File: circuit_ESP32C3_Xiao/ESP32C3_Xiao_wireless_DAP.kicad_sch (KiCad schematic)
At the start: 41 parts, among them J1 Cortex Debug 10pin connector, J2 ARM Standard JTAG, J3 Cortex Debug 10pin connector, J4 Conn_01x02, J6 Serial, Q1 ZXM61N03F, U1 XIAO-ESP32-C3-SMD, U2 AP1117-ADJ

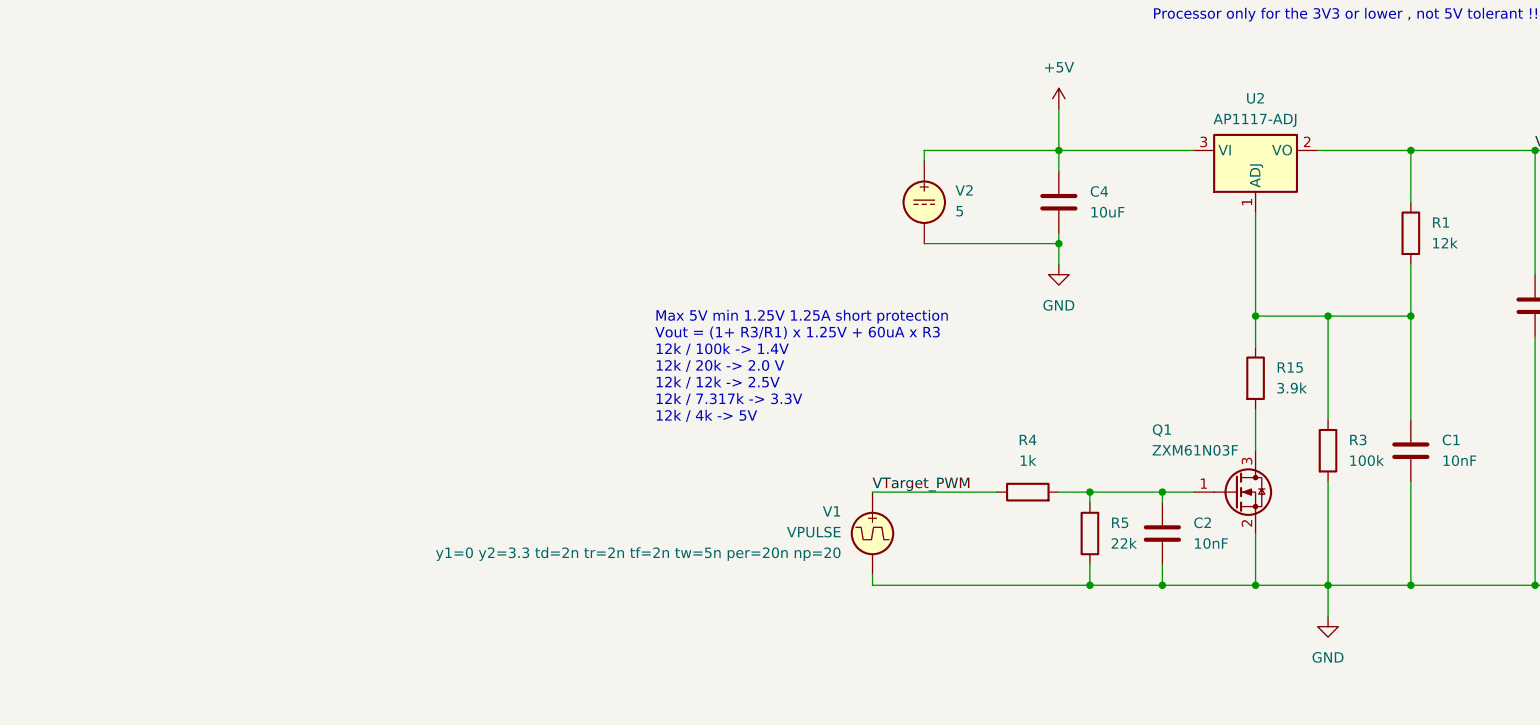
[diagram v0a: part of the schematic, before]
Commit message: Update the circuit, and create proper SPICE simulation model.
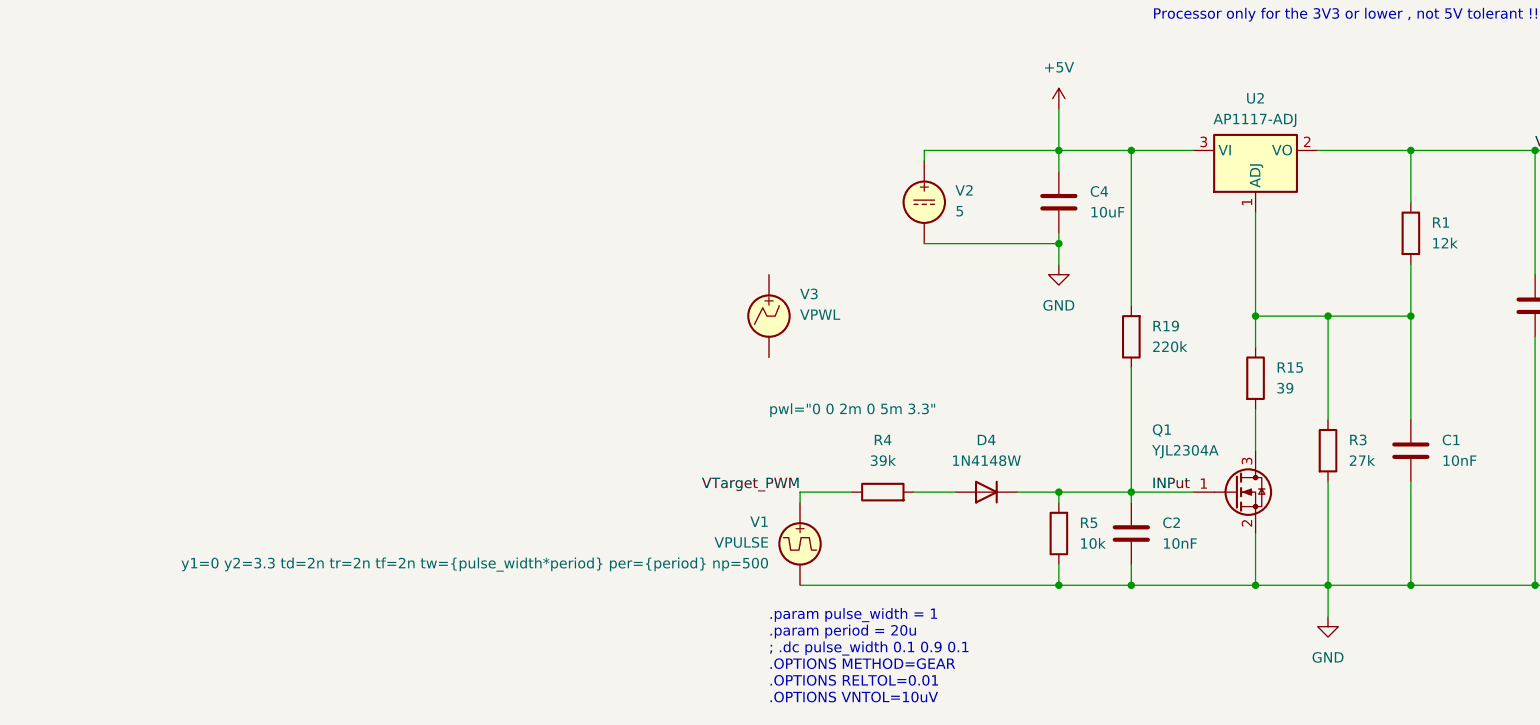
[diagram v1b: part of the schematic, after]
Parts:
- added D4: 1N4148W, Diode_SMD:D_SOD-123, symbol Diode:1N4148W
- added R19: 220k, Resistor_SMD:R_0603_1608Metric_Pad0.98x0.95mm_HandSolder, symbol Device:R
- added V3: VPWL, symbol Simulation_SPICE:VPWL
- Q1: value ZXM61N03F -> YJL2304A
- R15: value 3.9k -> 39
- R3: value 100k -> 27k
- R4: value 1k -> 39k
- R5: value 22k -> 10k
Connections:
- net +5V: now also R19.2
- net INPut: now reaches C2.1, Q1.1 (G), R5.2
- net INPut: now also D4.1 (K), R19.1; no longer R4.2
- new net: D4.2 (A), R4.2
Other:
- note added: ".param pulse_width = 1 .param period = 20u ; .dc pulse_width 0.1 0.9 0.1 .OPTIONS METHOD=GEAR .OPTIONS RELTOL=0.01 .OPTIONS VNTOL=10uV"
- note removed: "Max 5V min 1.25V 1.25A short protection Vout = (1+ R3/R1) x 1.25V + 60uA x R3 12k / 100k -> 1.4V 12k / 20k -> 2.0 V 12k / 12k -> 2.5V 12k / 7.317k -> 3.3V 12k / 4k -> 5V"
- moved on the sheet: C2, R4, R5, V1

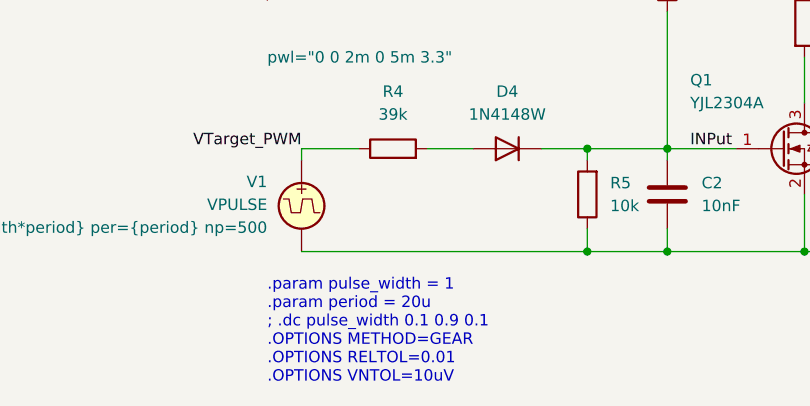
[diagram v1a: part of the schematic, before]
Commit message: Add VTarget linearity test suite with DMM integration
- Add test_vtarget_linearity.py: Comprehensive linearity testing with optional Keysight DMM reference
- Fix DAP_vendor.c ADC API compatibility: Convert ESP-IDF v5.0+ to v4.4.2 legacy API
- Update tests/README.md: Add DMM integration documentation and connection diagrams
- Fix GitHub Actions workflows: Remove continue-on-error and add proper error handling
- Expand CodeQL workflow: Add matrix for all 4 targets (esp8266, esp32, esp32c3, esp32s3)

Features:
- Dual measurement system: DAP + DMM reference for calibration
- Statistical analysis: R², linearity, DNL, INL metrics
- CSV export with DAP and DMM columns for traceability
- 3-panel visualization plots comparing DAP vs DMM
- Production-ready calibration capability
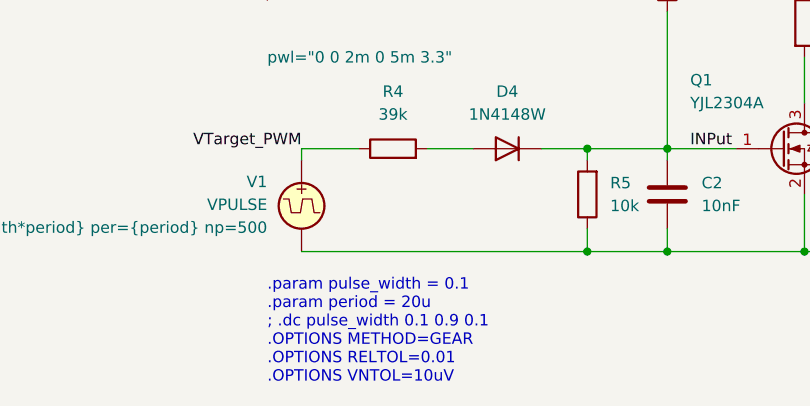
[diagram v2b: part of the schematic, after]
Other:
- note added: ".param pulse_width = 0.1 .param period = 20u ; .dc pulse_width 0.1 0.9 0.1 .OPTIONS METHOD=GEAR .OPTIONS RELTOL=0.01 .OPTIONS VNTOL=10uV"
- note removed: ".param pulse_width = 1 .param period = 20u ; .dc pulse_width 0.1 0.9 0.1 .OPTIONS METHOD=GEAR .OPTIONS RELTOL=0.01 .OPTIONS VNTOL=10uV"
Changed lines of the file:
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@@
 		)
 	)
-	(text ".param pulse_width = 1\n.param period = 20u\n; .dc pulse_width 0.1 0.9 0.1\n.OPTIONS METHOD=GEAR\n.OPTIONS RELTOL=0.01\n.OPTIONS VNTOL=10uV"
+	(text ".param pulse_width = 0.1\n.param period = 20u\n; .dc pulse_width 0.1 0.9 0.1\n.OPTIONS METHOD=GEAR\n.OPTIONS RELTOL=0.01\n.OPTIONS VNTOL=10uV"
 		(exclude_from_sim no)
 		(at 59.69 190.5 0)

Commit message: Add schematic SVG and LCSC verification tools
- Add ESP32C3 XIAO schematic diagram in SVG format to README
- Add analyze_components.py and verify_lcsc.py for LCSC part number validation
- Updated scripts to use relative paths for portability
- Updated KiCad schematic and PCB files with latest changes
- Updated BOM and gerber files for manufacturing
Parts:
- C1, C2, C5: LCSC C9900019212 -> C9900224280
- D4: LCSC (none) -> C2099
- J1: LCSC (none) -> C9900010269
- Q1: LCSC C9900145379 -> C699298
- R1, R16, R17: LCSC C93943 -> C114659
- R10, R11, R12, R13, R14, R8, R9: LCSC C9900206920 -> C114640
- R15: LCSC C11925 -> C2907032
- R18: LCSC C9900199398 -> C9900170064
- R19: LCSC C9900199398 -> C9900083237
- R2: LCSC C9900179919 -> C114640
- R3: LCSC C9900199399 -> C114614
- R4: LCSC C9900199398 -> C163424
- R5: LCSC C853859 -> C98220
- R6, R7: LCSC C9900199399 -> C22356636
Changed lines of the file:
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@@
 	(title_block
 		(title "Xiao_ESP32C3_wireless_DAP")
-		(date "2025-11-25")
+		(date "2025-12-29")
 		(rev "ver 0.1")
 	)
@@
 			)
 		)
-		(property "LCSC" "C93943"
+		(property "LCSC" "C114659"
 			(at 170.18 160.0199 0)
 			(effects
@@
 			)
 		)
-		(property "LCSC" "C9900199398"
+		(property "LCSC" "C163424"
 			(at 73.66 163.83 0)
 			(effects
@@
 			)
 		)
-		(property "LCSC" "C9900206920"
+		(property "LCSC" "C114640"
 			(at 52.07 60.96 0)
 			(effects
@@
 			)
 		)
-		(property "LCSC" "C93943"
+		(property "LCSC" "C114659"
 			(at 260.35 135.8899 0)
 			(effects
@@
 			)
 		)
+		(property "LCSC" "C9900010269"
+			(at 231.14 31.75 0)
+			(effects
+				(font
+					(size 1.27 1.27)
+				)
+				(hide yes)
+			)
+		)
 		(pin "7"
 		)
@@
 			)
 		)
-		(property "LCSC" "C9900206920"
+		(property "LCSC" "C114640"
 			(at 52.07 57.15 0)
 			(effects
@@
 			)
 		)
-		(property "LCSC" "C9900199399"
+		(property "LCSC" "C22356636"
 			(at 234.95 128.27 0)
 			(effects
@@
 			)
 		)
-		(property "LCSC" "C9900206920"
+		(property "LCSC" "C114640"
 			(at 52.07 68.58 0)
 			(effects
@@
 			)
 		)
-		(property "LCSC" "C9900145379"
+		(property "LCSC" "C699298"
 			(at 106.68 162.56 0)
 			(effects
@@
 			)
 		)
-		(property "LCSC" "C9900199399"
+		(property "LCSC" "C22356636"
 			(at 234.95 140.97 0)
 			(effects
@@
 			)
 		)
+		(property "LCSC" "C2099"
+			(at 86.36 163.83 0)
+			(effects
+				(font
+					(size 1.27 1.27)
+				)
+				(hide yes)
+			)
+		)
 		(pin "1"
 		)
@@
 			)
 		)
-		(property "LCSC" "C853859"
+		(property "LCSC" "C98220"
 			(at 97.79 173.9899 0)
 			(effects
@@
 			)
 		)
-		(property "LCSC" "C9900199398"
+		(property "LCSC" "C9900170064"
 			(at 144.78 77.4699 0)
 			(effects
@@
 			)
 		)
-		(property "LCSC" "C9900019212"
+		(property "LCSC" "C9900224280"
 			(at 142.24 163.8299 0)
 			(effects
@@
 			)
 		)
-		(property "LCSC" "C9900206920"
+		(property "LCSC" "C114640"
 			(at 52.07 64.77 0)
 			(effects
@@
 			)
 		)
-		(property "LCSC" "C9900019212"
+		(property "LCSC" "C9900224280"
 			(at 248.92 139.6999 0)
 			(effects
@@
 			)
 		)
-		(property "LCSC" "C11925"
+		(property "LCSC" "C2907032"
 			(at 121.92 154.9399 0)
 			(effects
@@
 			)
 		)
-		(property "LCSC" "C9900199398"
+		(property "LCSC" "C9900083237"
 			(at 97.79 151.13 0)
 			(effects
@@
 			)
 		)
-		(property "LCSC" "C9900019212"
+		(property "LCSC" "C9900224280"
 			(at 107.95 173.9899 0)
 			(effects
@@
 			)
 		)
-		(property "LCSC" "C9900206920"
+		(property "LCSC" "C114640"
 			(at 111.76 68.58 0)
 			(effects
@@
 			)
 		)
-		(property "LCSC" "C9900206920"
+		(property "LCSC" "C114640"
 			(at 52.07 72.39 0)
 			(effects
@@
 			)
 		)
-		(property "LCSC" "C93943"
+		(property "LCSC" "C114659"
 			(at 140.97 137.1599 0)
 			(effects
@@
 			)
 		)
-		(property "LCSC" "C9900206920"
+		(property "LCSC" "C114640"
 			(at 111.76 72.39 0)
 			(effects
@@
 			)
 		)
-		(property "LCSC" "C9900179919"
+		(property "LCSC" "C114640"
 			(at 111.76 64.77 0)
 			(effects
@@
 			)
 		)
-		(property "LCSC" "C9900199399"
+		(property "LCSC" "C114614"
 			(at 130.81 163.8299 0)
 			(effects

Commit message: kicad: update ESP32C3 XIAO design + fabrication outputs
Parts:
- C1, C2, C5: TME (none) -> 0603B103K500CG
- C3, C4, C6: TME (none) -> CS2012X7R106M100NR
- D1, D3: TME (none) -> OSDR0603C1E
- D2: TME (none) -> OSHR0603Z74A
- D4: TME (none) -> 1N4148W-TP
- J1: TME (none) -> ZL262-10
- J2: LCSC (none) -> C109409; TME (none) -> DS1013-20RSIB
- J3: TME (none) -> ZL262-10G
- J4: LCSC (none) -> C124375; TME (none) -> ZL201-2G
- J6: LCSC (none) -> C180248; TME (none) -> ZL201-3G
- Q1: TME (none) -> 2N7002K.T
- R1, R16, R17: TME (none) -> RC0603JR-0712KL
- R10, R11, R12, R13, R14, R2, R8, R9: TME (none) -> RC0603JR-07120RL
- R15: TME (none) -> RC0603JR-0739RL
- R18: TME (none) -> RC0603JR-071KL
- R19: TME (none) -> RC0603JR-07220KL
- R3: TME (none) -> RC0603JR-0727KL
- R4: TME (none) -> RC0603JR-0739KL
- R5: TME (none) -> RC0603JR-0710KL
- R6, R7: TME (none) -> RC0603JR-07100KL
- U1: TME (none) -> 102991-XIAO-ESP32C3
- U2: TME (none) -> LDI1117-ADJ
